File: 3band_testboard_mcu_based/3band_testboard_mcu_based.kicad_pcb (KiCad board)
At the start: 2 copper layers, 88.9 x 72.6 mm, 52 parts, among them J1 Conn_Coaxial, J2 Conn_Coaxial, J3 Conn_Coaxial, J4 1140084168, J5 Battery in, J6 USB_C_Receptacle_USB2.0_16P, U1 RFM96W-433S2, U2 AMS1117-3.3, U3 AMS1117-3.3, U4 LBAA0XV2GT-001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

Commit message: Færdiggjorde GPIO
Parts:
- added C14: 100n, Capacitor_SMD:C_0603_1608Metric, F.Cu at (97.5, 83.1)
- added C15: 100n, Capacitor_SMD:C_0603_1608Metric, F.Cu at (141.2, 96.3)
- added C16: 10n, Capacitor_SMD:C_0603_1608Metric, F.Cu at (91.4, 77.0)
- added C17: 100n, Capacitor_SMD:C_0603_1608Metric, F.Cu at (113.3, 54.4)
- added C18: 100p, Capacitor_SMD:C_0603_1608Metric_Pad1.08x0.95mm_HandSolder, F.Cu at (130.4, 50.5)
- added J7: UART header, Connector_PinSocket_2.54mm:PinSocket_1x06_P2.54mm_Vertical, F.Cu at (101.3, 76.5)
- added J8: Free GPIO, Connector_PinHeader_2.54mm:PinHeader_1x06_P2.54mm_Vertical, F.Cu at (101.3, 83.1)
- added J9: CS_enable, Connector_PinHeader_2.54mm:PinHeader_2x02_P2.54mm_Vertical, F.Cu at (110.2, 59.7)
- added L1: 15u, Inductor_SMD:L_Murata_DFE201610P, F.Cu at (144.0, 97.8)
- added Q1: BC846, Package_TO_SOT_SMD:SOT-23, F.Cu at (111.8, 71.4)
- added Q2: BC846, Package_TO_SOT_SMD:SOT-23, F.Cu at (111.8, 67.6)
- added R15: 10k, Resistor_SMD:R_0603_1608Metric, F.Cu at (114.6, 69.3)
- added R16: 10k, Resistor_SMD:R_0603_1608Metric, F.Cu at (109.0, 69.3)
- added R17: 10k, Resistor_SMD:R_0603_1608Metric, F.Cu at (115.1, 54.3)
- added TP9: Vreg, TestPoint:TestPoint_Pad_D1.5mm, F.Cu at (141.2, 99.3)
- moved TP4 35.6 mm to (151.6, 33.3)
- moved TP1 19.4 mm to (124.2, 43.7)
- moved C6 8.86 mm to (135.1, 87.1), turned to 180 degrees
- moved TP7 7.15 mm to (124.2, 46.7)
- moved C4 5.68 mm to (86.9, 40.6), turned to 90 degrees
- moved R10 4.91 mm to (84.8, 40.7), turned to -90 degrees
- moved R11 2.59 mm to (83.3, 40.6), turned to 90 degrees
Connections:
- net Net-(U5-EN) renamed /MCU/ESP32.enable
- U1 pad 5: /433MHz/~{cs} -> /CS1
- U4 pad 10: /800_2400MHz/~{CS} -> /CS2
- U4 pad 11: /800_2400MHz/MISO -> /433MHz/MISO
- U4 pad 12: /800_2400MHz/MOSI -> /433MHz/MOSI
- U4 pad 13: /800_2400MHz/SCK -> /433MHz/SCK
- U4 pad 4: unconnected-(U4-VREG-Pad4) -> Net-(U4-VREG)
- U4 pad 6: unconnected-(U4-DCC_SW-Pad6) -> Net-(U4-DCC_SW)
- U5 pad 10: unconnected-(U5-IO17-Pad10) -> /433MHz/MOSI
- U5 pad 11: unconnected-(U5-IO18-Pad11) -> /433MHz/SCK
- U5 pad 17: unconnected-(U5-IO9-Pad17) -> /MCU/GPIO.9
- U5 pad 18: unconnected-(U5-IO10-Pad18) -> /MCU/GPIO.10
- U5 pad 19: unconnected-(U5-IO11-Pad19) -> /MCU/GPIO.11
- U5 pad 20: unconnected-(U5-IO12-Pad20) -> /MCU/GPIO.12
- U5 pad 21: unconnected-(U5-IO13-Pad21) -> /MCU/GPIO.13
- U5 pad 24: unconnected-(U5-IO47-Pad24) -> /MCU/~{CS1}
- U5 pad 25: unconnected-(U5-IO48-Pad25) -> /MCU/~{CS2}
- U5 pad 27: unconnected-(U5-IO0-Pad27) -> /MCU/ESP32.reset
- U5 pad 4: unconnected-(U5-IO4-Pad4) -> /MCU/SD.detect
- U5 pad 5: unconnected-(U5-IO5-Pad5) -> /MCU/SD.DO
- U5 pad 6: unconnected-(U5-IO6-Pad6) -> /MCU/SD.SCK
- U5 pad 7: unconnected-(U5-IO7-Pad7) -> /MCU/SD.DI
- U5 pad 8: unconnected-(U5-IO15-Pad8) -> /MCU/~{SD.CS}
- U5 pad 9: unconnected-(U5-IO16-Pad9) -> /433MHz/MISO
- U7 pad 11: unconnected-(U7-CTS-Pad11) -> /MCU/UART.CTS
- U7 pad 2: unconnected-(U7-DTR-Pad2) -> /MCU/UART.DTR
- U7 pad 3: unconnected-(U7-RTS-Pad3) -> /MCU/UART.RTS
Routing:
- net /433MHz/MISO: track 0.00 -> 132.8 mm, vias 0 -> 6
- net /433MHz/MOSI: track 0.00 -> 130.1 mm, vias 0 -> 6
- net /433MHz/SCK: track 0.00 -> 127.0 mm, vias 0 -> 6
- net /CS2: track 0.00 -> 61.7 mm, vias 0 -> 2
- net /CS1: track 0.00 -> 53.1 mm, vias 0 -> 2
- net /MCU/ESP32.enable: track 4.89 -> 53.2 mm, vias 0 -> 2
- net /MCU/GPIO.13: track 0.00 -> 41.2 mm, vias 0 -> 1
- net /MCU/UART.TX: track 0.00 -> 40.0 mm, vias 0 -> 2
- net /MCU/GPIO.12: track 0.00 -> 39.0 mm, vias 0 -> 1
- net +3.3V: track 49.1 -> 86.7 mm, vias 57 -> 59
- net /MCU/GPIO.11: track 0.00 -> 36.7 mm, vias 0 -> 1
- net /MCU/GPIO.10: track 0.00 -> 34.5 mm, vias 0 -> 1
- net /MCU/GPIO.9: track 0.00 -> 32.3 mm, vias 0 -> 1
- net /MCU/ESP32.reset: track 0.00 -> 19.2 mm, vias 0 -> 2
- net /MCU/SD.DI: track 0.00 -> 17.8 mm
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- added copper zone on F.Cu, net Net-(U4-VREG)

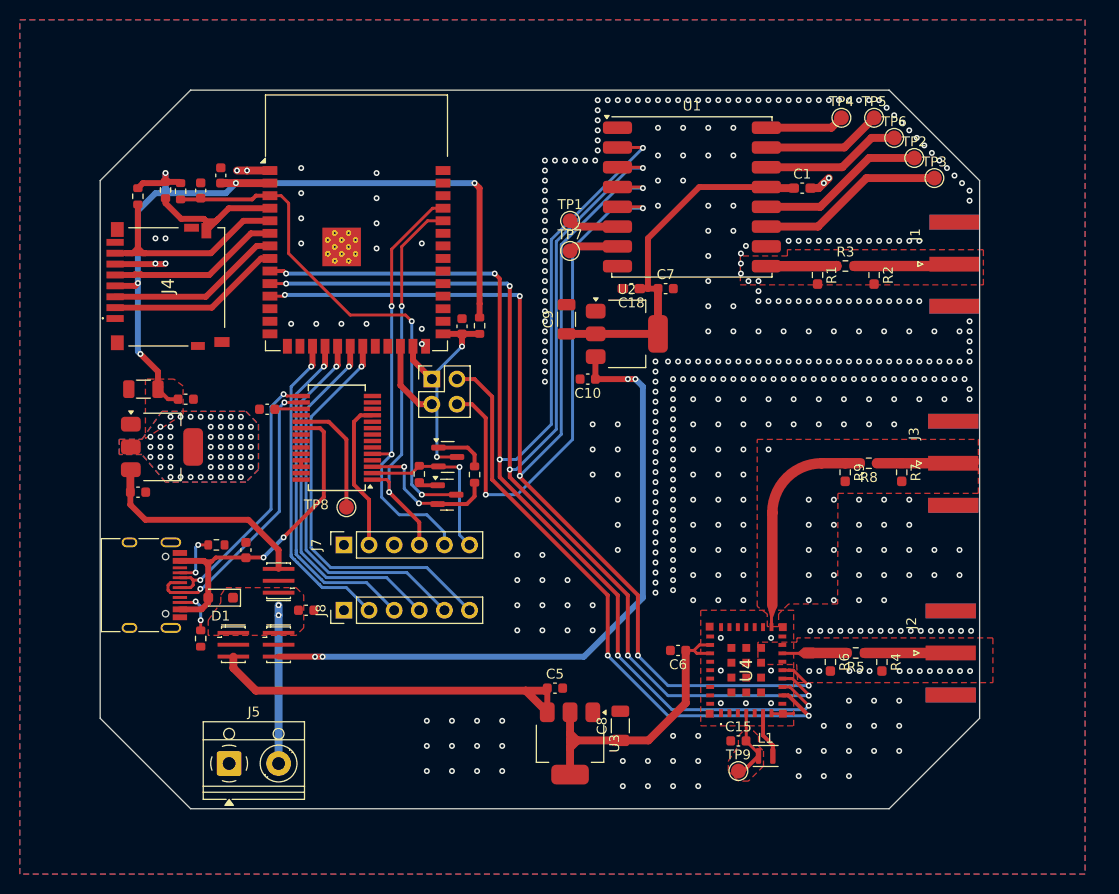
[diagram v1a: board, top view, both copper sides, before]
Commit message: DRC check, and price
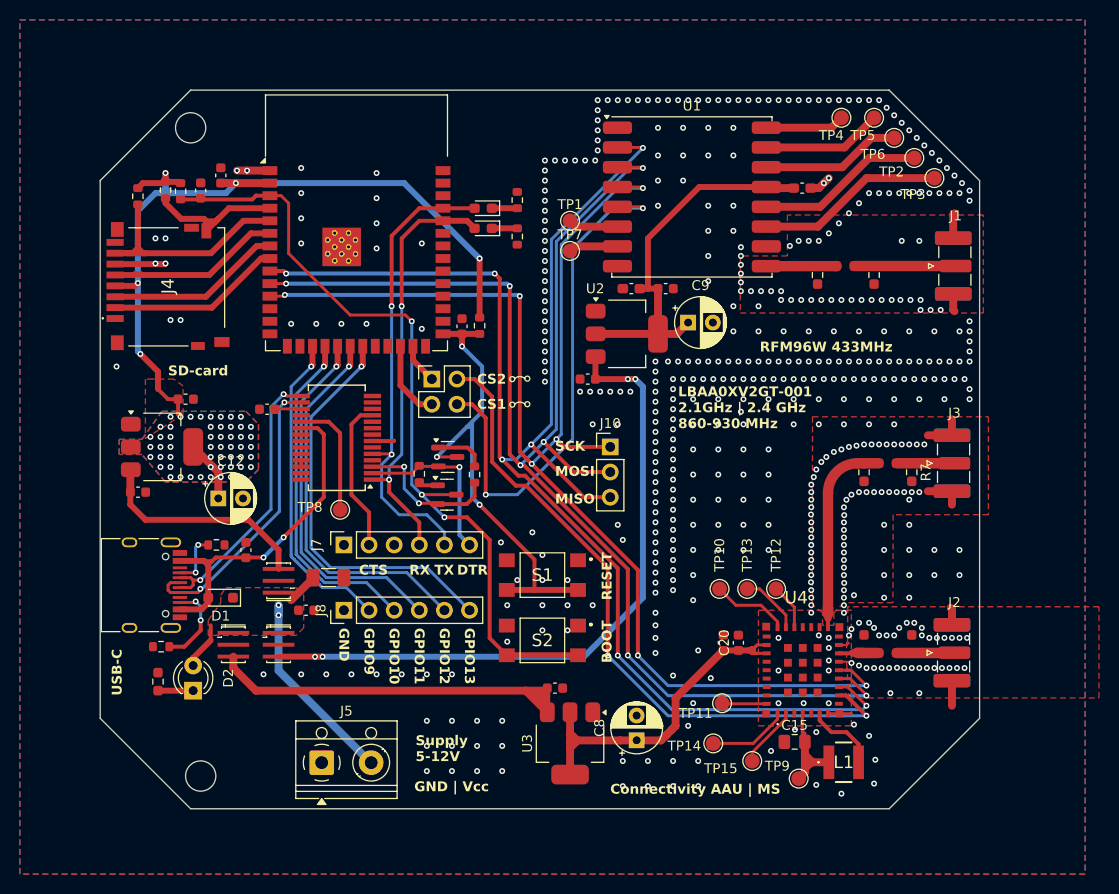
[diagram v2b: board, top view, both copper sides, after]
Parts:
- added C19: 2u, Capacitor_SMD:C_1206_3216Metric_Pad1.33x1.80mm_HandSolder, F.Cu at (99.8, 79.8)
- added C20: 100p, Capacitor_SMD:C_0603_1608Metric, F.Cu at (141.2, 86.3)
- added D2: LED, LED_THT:LED_D3.0mm, F.Cu at (86.1, 91.2)
- added D3: LED, LED_SMD:LED_0603_1608Metric_Pad1.05x0.95mm_HandSolder, F.Cu at (115.4, 42.4)
- added D4: LED, LED_SMD:LED_0603_1608Metric_Pad1.05x0.95mm_HandSolder, F.Cu at (115.4, 44.5)
- added J10: SPI debug, Connector_PinHeader_2.54mm:PinHeader_1x03_P2.54mm_Vertical, F.Cu at (128.3, 66.5)
- added R18: 1k, Resistor_SMD:R_0603_1608Metric_Pad0.98x0.95mm_HandSolder, F.Cu at (82.5, 90.3)
- added R19: 680, Resistor_SMD:R_0603_1608Metric, F.Cu at (118.9, 41.6)
- added R20: 680, Resistor_SMD:R_0603_1608Metric, F.Cu at (118.9, 45.3)
- added S1: TL3305BF100QG, Tactile_switch:TL3305BF160QG, F.Cu at (121.4, 79.5)
- added S2: TL3305BF100QG, Tactile_switch:TL3305BF160QG, F.Cu at (121.4, 86.1)
- added TP10: RFSW2, TestPoint:TestPoint_Pad_D1.5mm, F.Cu at (139.3, 80.9)
- added TP11: RST, TestPoint:TestPoint_Pad_D1.5mm, F.Cu at (139.6, 92.5)
- added TP12: RFSW0, TestPoint:TestPoint_Pad_D1.5mm, F.Cu at (145.0, 80.9)
- added TP13: RFSW1, TestPoint:TestPoint_Pad_D1.5mm, F.Cu at (142.1, 80.9)
- added TP14: DIO9, TestPoint:TestPoint_Pad_D1.5mm, F.Cu at (138.7, 96.5)
- added TP15: DIO8, TestPoint:TestPoint_Pad_D1.5mm, F.Cu at (142.6, 98.3)
- C12, C8, C9: footprint Capacitor_SMD:C_1206_3216Metric -> Capacitor_THT:CP_Radial_D5.0mm_P2.50mm
- C15: value 100n -> 470n; footprint Capacitor_SMD:C_0603_1608Metric -> Capacitor_SMD:C_0805_2012Metric_Pad1.18x1.45mm_HandSolder
- J1, J2, J3: footprint Connector_Coaxial:SMA_Amphenol_132289_EdgeMount -> Connector_Coaxial:SMA_Samtec_SMA-J-P-H-ST-EM1_EdgeMount
- L1: footprint Inductor_SMD:L_Murata_DFE201610P -> Inductor:ASPI-4030S
- moved C12 13.4 mm to (88.6, 71.8), turned to 0 degrees
- moved C9 12.3 mm to (136.1, 54.0), turned to 0 degrees
- moved J5 9.36 mm to (99.1, 98.5)
- moved L1 7.91 mm to (151.9, 98.4)
- moved TP9 6.14 mm to (147.3, 100.1), turned to 180 degrees
- moved U4 5.72 mm to (147.7, 89.1)
- moved C15 5.69 mm to (146.9, 96.4)
- moved C6 4.64 mm to (139.7, 86.3), turned to 90 degrees
- moved R14 4.09 mm to (82.9, 86.7), turned to 0 degrees
- moved R6 3.86 mm to (153.9, 86.5), turned to 90 degrees
- moved R4 3.53 mm to (158.8, 86.5), turned to 90 degrees
- moved R5 3.23 mm to (156.3, 87.4)
- moved C8 2.20 mm to (130.9, 96.2)
- moved R8 1.91 mm to (156.3, 68.2)
- moved R9 1.91 mm to (153.9, 69.1)
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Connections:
- U4 pad 1: unconnected-(U4-DIO9-Pad1) -> Net-(U4-DIO9)
- U4 pad 2: unconnected-(U4-DIO8-Pad2) -> Net-(U4-DIO8)
- U4 pad 20: unconnected-(U4-GND_8-Pad20) -> GND
- U4 pad 23: unconnected-(U4-RFSW0-Pad23) -> Net-(U4-RFSW0)
- U4 pad 24: unconnected-(U4-RFSW1-Pad24) -> Net-(U4-RFSW1)
- U4 pad 25: unconnected-(U4-RFSW2-Pad25) -> Net-(U4-RFSW2)
- U4 pad 35: unconnected-(U4-LR_NRST-Pad35) -> Net-(U4-LR_NRST)
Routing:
- net /MCU/ESP32.reset: track 19.2 -> 48.3 mm, vias 2 -> 3
- net /MCU/ESP32.enable: track 53.2 -> 81.5 mm, vias 2 -> 3
- net GND: track 13.2 -> 36.4 mm, vias 444 -> 524
- net /433MHz/MISO: track 132.8 -> 149.0 mm, vias 6 -> 7
- net VCC: track 16.0 -> 28.8 mm
- net /433MHz/MOSI: track 130.1 -> 142.9 mm, vias 6 -> 7
- net /433MHz/SCK: track 127.0 -> 136.9 mm, vias 6 -> 7
- net Net-(U4-DIO9): track 0.00 -> 8.83 mm
- net 3.3V RF2: track 31.5 -> 39.4 mm
- net Net-(U4-RFSW2): track 0.00 -> 7.78 mm
- net /CS2: track 61.7 -> 68.1 mm
- net Net-(U4-VREG): track 7.28 -> 13.6 mm
- net Net-(U4-DIO8): track 0.00 -> 6.25 mm
- net Net-(U4-RFSW1): track 0.00 -> 6.23 mm
- net Net-(U4-RFSW0): track 0.00 -> 4.63 mm
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- removed copper zone on F.Cu, net Net-(U4-VREG)
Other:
- outline, holes or cut-outs redrawn
- board text added: "BOOT"
- board text added: "CS1"
- board text added: "CS2"
- board text added: "CTS"
- board text added: "Connectivity AAU | MS"
- board text added: "DTR"
- board text added: "GND"
- board text added: "GND | Vcc"
- board text added: "GPIO10"
- board text added: "GPIO11"
- board text added: "GPIO12"
- board text added: "GPIO13"
- board text added: "GPIO9"
- board text added: "LBAA0XV2GT-001 2.1GHz | 2.4 GHz 860-930 MHz"
- board text added: "MISO"
- board text added: "MOSI"
- board text added: "RESET"
- board text added: "RFM96W 433MHz"
- board text added: "RX"
- board text added: "SCK"
- board text added: "SD-card"
- board text added: "Supply 5-12V"
- board text added: "TX"
- board text added: "USB-C"
- board text removed: "ESP32 -- FT232"
